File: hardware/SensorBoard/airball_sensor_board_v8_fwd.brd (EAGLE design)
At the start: 5.6 x 9.2 mm, 60 parts, among them IC1 CP2102, J2 USB Female Type C Connector, T1 BC846, T2 BC846, U1 BQ24075, U2 BQ27441-G1, U3 BMP388, U4 ESP-WROOM-32

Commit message: Finished initial design and routing.
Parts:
- removed FID1, FID2, FID3, FID4, FID5, FID6: FIDUCIAL1X2, SparkFun-Aesthetics:FIDUCIAL-1X2
- removed FRAME1, FRAME2: FRAME-LETTER, SparkFun-Aesthetics:CREATIVE_COMMONS
- removed R11: (no value), SparkFun-Resistors:1206
- removed STANDOFF1, STANDOFF10, STANDOFF11, STANDOFF12, STANDOFF2, STANDOFF3, STANDOFF4, STANDOFF5, STANDOFF6, STANDOFF7, STANDOFF8, STANDOFF9: STAND-OFF, SparkFun-Electromechanical:STAND-OFF
- added C10: 10uF, SparkFun-Capacitors:0603
- added C11, C925, C926, C927: 4.7uF, SparkFun-Capacitors:0603
- added C8, C9: 0.1uF, SparkFun-Capacitors:0603
- added R17: 0.01, SparkFun-Resistors:1206
- added U7: SP0503BAHT, SP0503BAHT:SOT143
- R3: value 2.0k -> 1k
- moved FRAME3 148.2 mm to (8.26, -10.2)
- moved R12 132.2 mm to (36.8, 26.4), turned to 180 degrees
- moved R10 130.8 mm to (36.8, 28.3), turned to 180 degrees
- moved R14 121.8 mm to (9.53, 4.13), turned to 270 degrees
- moved R13 120.3 mm to (15.6, 4.13), turned to 270 degrees
- moved T2 116.0 mm to (18.4, 4.13), turned to 180 degrees
- moved U3 112.3 mm to (71.1, 4.45)
- moved T1 106.9 mm to (12.7, 4.13), turned to 180 degrees
- moved U4 100.0 mm to (33.3, 12.1)
- moved C6 77.5 mm to (29.8, 27.3)
- moved R4 68.4 mm to (10.8, 16.8), turned to 270 degrees
- moved R6 68.4 mm to (10.8, 13.3), turned to 90 degrees
- moved C7 62.9 mm to (14.0, 16.2), turned to 180 degrees
- moved J1 60.0 mm to (85.7, 31.4), turned to 90 degrees
- moved R3 58.5 mm to (10.8, 9.53), turned to 90 degrees
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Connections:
- net N$1 renamed MISO
- net N$10 renamed SS_27
- net N$2 renamed SCLK
- net N$6 renamed SS_25
- net N$9 renamed SS_26
- removed net VDD: U3.10
- new net N$14: C6.1, U2.5
- net BATTERY_IN: now also R17.2; no longer R11.2
- net GND: now also C10.2, C11.2, C8.2, C9.2, C925.2, C926.2, C927.2, J1.1, U7.1; no longer J1.2
- net USB_D+: now also U7.3
- net USB_D-: now also U7.2
- net VCC: now also C10.1, C11.1, C8.1, C9.1, C925.1, C926.1, C927.1, J1.2, U3.10; no longer C6.1, J1.1, R3.2, U2.5
- net V_BATT: now also R17.1; no longer R11.1
- net V_USB: now also R3.2, U7.4
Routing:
- net VCC: track 52.9 -> 186.2 mm, vias 2 -> 7
- net SDA: track 0.00 -> 128.1 mm, vias 0 -> 4
- net SCL: track 0.00 -> 125.0 mm, vias 0 -> 6
- net MISO: track 0.00 -> 75.6 mm, vias 0 -> 2
- net SCLK: track 0.00 -> 71.3 mm, vias 0 -> 4
- net V_USB: track 11.0 -> 68.6 mm, vias 0 -> 2
- net SS_26: track 0.00 -> 41.9 mm, vias 0 -> 2
- net N$12: track 0.00 -> 39.5 mm, vias 0 -> 2
- net USB_D-: track 0.00 -> 31.4 mm, vias 0 -> 2
- net SS_27: track 0.00 -> 29.6 mm, vias 0 -> 2
- net USB_D+: track 0.00 -> 29.5 mm, vias 0 -> 2
- net V_BATT: track 8.99 -> 37.5 mm, vias 0 -> 2
- net USB_RXD: track 0.00 -> 26.2 mm, vias 0 -> 2
- net USB_TXD: track 0.00 -> 26.1 mm, vias 0 -> 2
- net BATTERY_IN: track 21.9 -> 47.9 mm, vias 2 -> 3
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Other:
- board text added: "Ihab Awad"

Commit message: Applied design rules and improved the board.
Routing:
- net GND: track 0.00 -> 20.0 mm, vias 0 -> 7
- net BATTERY_IN: track 47.9 -> 51.1 mm
- net USB_D+: track 29.5 -> 31.7 mm
- net USB_D-: track 31.4 -> 33.5 mm
- net V_BATT: track 37.5 -> 38.7 mm
- net V_USB: track 68.6 -> 69.6 mm
- net N$13: track 8.90 -> 8.87 mm, vias 1 -> 2
- added copper zone on layer 1, net GND
- added copper zone on layer 16, net GND

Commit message: More routing and design.
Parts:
- added D2: GREEN, SparkFun-LED:LED-0603
- added D3: Yellow, SparkFun-LED:LED-0603
- added D4: RED, SparkFun-LED:LED-0603
- added R11: 180, SparkFun-Resistors:0603-RES
- added R18: 10K, SparkFun-Resistors:0603-RES
- added R19: 750, SparkFun-Resistors:0603-RES
- R5: value 590 -> 898
- R7: value 1.1k -> 1.54k
- R8: value 100k -> 750
- U$925, U$926, U$927: value HONEYWELL_HSC_SMT -> (none)
- moved U$926 90.6 mm to (157.8, 47.3)
- moved C11 90.6 mm to (156.5, 21.9)
- moved C925 90.6 mm to (146.4, 52.4)
- moved C926 90.6 mm to (164.5, 52.4)
- moved C927 90.6 mm to (147.0, 32.4)
- moved J1 90.6 mm to (174.6, 48.9)
- moved U$927 90.6 mm to (140.3, 27.3)
- moved U3 90.6 mm to (160.0, 21.9)
- moved U$925 90.6 mm to (139.7, 47.3)
- moved FRAME3 57.3 mm to (65.4, -14.6)
- moved R9 34.1 mm to (31.4, 2.54), turned to 270 degrees
- moved R8 30.9 mm to (33.3, 2.54), turned to 270 degrees
- moved D1 28.8 mm to (31.4, 6.03), turned to 270 degrees
- moved C2 28.1 mm to (10.2, 2.54)
- moved R10 27.7 mm to (25.7, 2.86), turned to 90 degrees
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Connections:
- net N$3 renamed SYSOFF_PULLUP
- removed net !CE!: R8.1, U1.4
- removed net EN1: R16.2, U1.6
- new net N$1: D4.A, U4.9
- new net N$19: R11.2, U1.7
- new net N$2: D4.C, R19.1
- new net N$20: D2.C, R11.1
- new net N$21: R16.2, U1.5
- new net N$22: D3.C, R8.1
- new net N$23: R18.2, U2.10
- net GND: now also R18.1, R19.2, U1.4, U1.6; no longer U1.5
- net TS: no longer U2.10
- net VCC: now also D3.A
- net V_SUPPLY_UNREG: now also D2.A
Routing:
- net VCC: track 185.8 -> 65.4 mm, vias 7 -> 0
- net SDA: track 127.9 -> 9.54 mm, vias 4 -> 0
- net SCL: track 125.3 -> 8.37 mm, vias 6 -> 0
- net MISO: track 75.8 -> 0.00 mm, vias 2 -> 0
- net SCLK: track 71.7 -> 0.00 mm, vias 4 -> 0
- net SS_26: track 42.3 -> 0.00 mm, vias 2 -> 0
- net BATTERY_IN: track 51.1 -> 13.9 mm, vias 3 -> 6
- net SS_27: track 29.9 -> 0.00 mm, vias 2 -> 0
- net V_BATT: track 38.7 -> 9.65 mm, vias 2 -> 0
- net SYSOFF_PULLUP: track 3.14 -> 29.9 mm, vias 0 -> 2
- net N$13: track 8.87 -> 33.5 mm
- net SS_25: track 22.1 -> 0.00 mm, vias 2 -> 0
- net N$12: track 39.7 -> 19.6 mm
- net V_SUPPLY_UNREG: track 26.2 -> 6.69 mm
- net !CHG!: track 3.32 -> 21.8 mm, vias 0 -> 2
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- added copper zone on layer 1, net BATTERY_IN
- added copper zone on layer 16, net BATTERY_IN
- added copper zone on layer 1, net V_BATT
- added copper zone on layer 1, net V_SUPPLY_UNREG
- added copper zone on layer 1, net V_USB
- removed copper zone on layer 1, net GND
- removed copper zone on layer 16, net GND

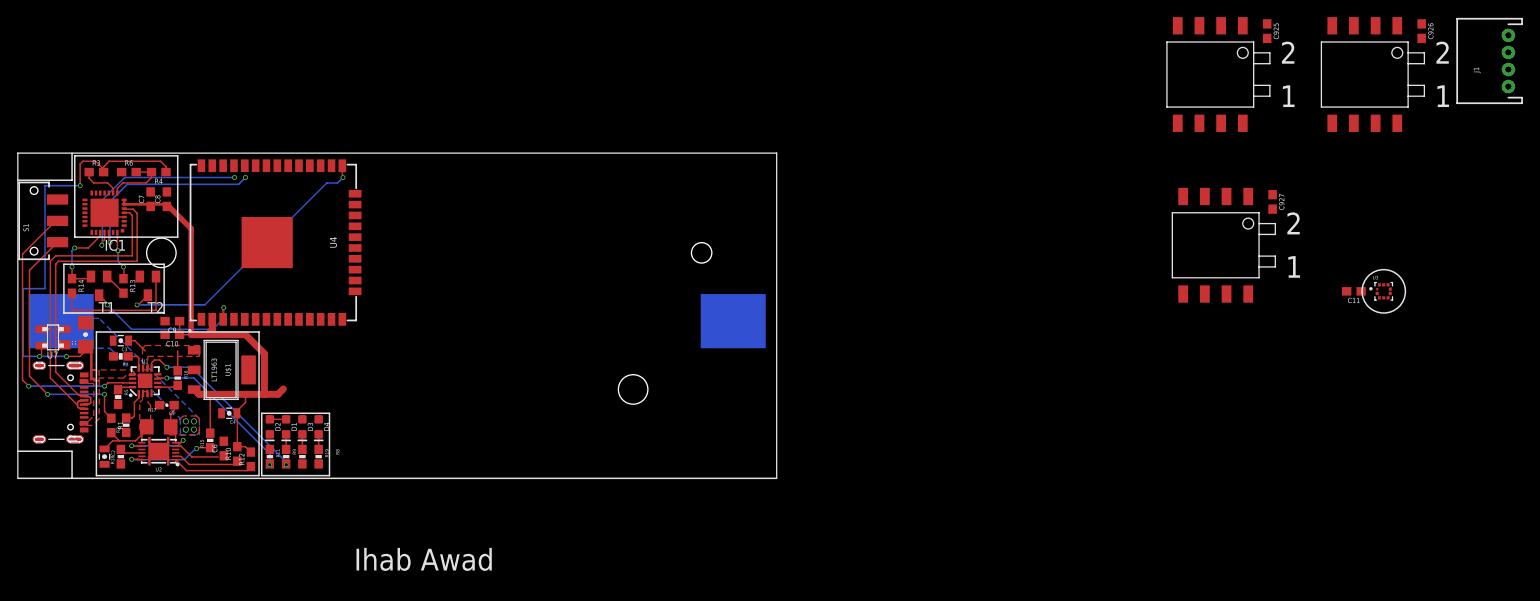
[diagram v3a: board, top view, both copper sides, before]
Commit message: Finished routing board; ground planes still not done.
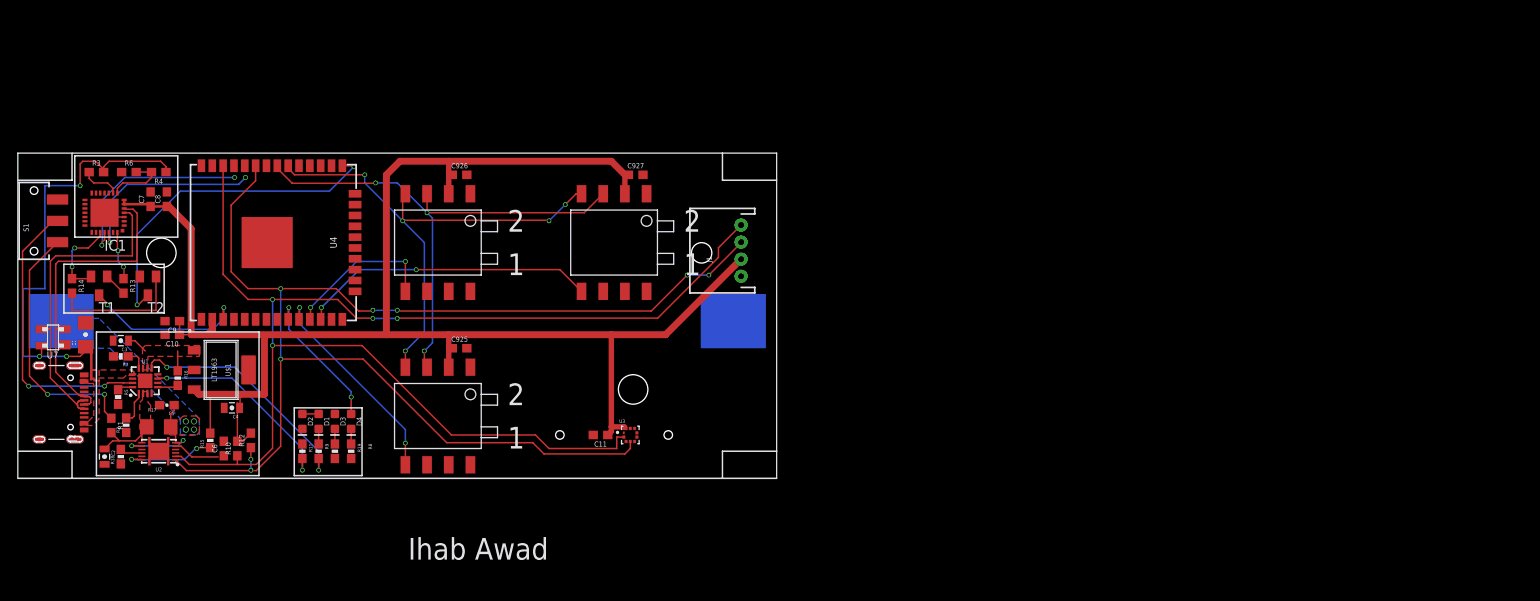
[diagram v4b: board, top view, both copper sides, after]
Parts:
- moved C926 114.0 mm to (51.8, 35.6), turned to 0 degrees
- moved U$926 110.4 mm to (49.2, 27.6)
- moved C925 101.6 mm to (51.8, 15.2), turned to 0 degrees
- moved U$925 98.9 mm to (49.2, 7.30)
- moved J1 92.6 mm to (84.7, 26.7)
- moved U3 89.9 mm to (71.8, 5.08)
- moved C11 89.9 mm to (68.3, 5.08)
- moved C927 74.7 mm to (72.4, 35.6), turned to 0 degrees
- moved U$927 70.5 mm to (69.8, 27.6)
- moved FRAME3 50.5 mm to (15.2, -8.57)
- moved D3 3.86 mm to (37.1, 6.67)
- moved D4 3.86 mm to (39.1, 6.67)
- moved R19 3.86 mm to (39.1, 3.17)
- moved R8 3.86 mm to (37.1, 3.17)
- moved D1 3.86 mm to (35.2, 6.67)
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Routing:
- net SDA: track 9.54 -> 160.5 mm, vias 0 -> 8
- net SCL: track 8.37 -> 159.3 mm, vias 0 -> 4
- net VCC: track 65.4 -> 195.0 mm
- net MISO: track 0.00 -> 62.7 mm, vias 0 -> 3
- net SCLK: track 0.00 -> 61.6 mm, vias 0 -> 5
- net SS_27: track 0.00 -> 34.8 mm, vias 0 -> 2
- net SS_25: track 0.00 -> 25.0 mm, vias 0 -> 2
- net SS_26: track 0.00 -> 18.3 mm, vias 0 -> 2
- net N$1: track 0.00 -> 16.9 mm, vias 0 -> 2
- net N$13: track 33.5 -> 40.1 mm
- net !CHG!: track 21.8 -> 28.4 mm
- net N$19: track 18.1 -> 24.3 mm

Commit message: Updated descriptions and documentation.
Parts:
- added FRAME1, FRAME2: FRAME-LETTER, SparkFun-Aesthetics:CREATIVE_COMMONS
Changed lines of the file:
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@@
 <layer number="14" name="Route14" color="1" fill="6" visible="no" active="no"/>
 <layer number="15" name="Route15" color="4" fill="6" visible="no" active="no"/>
-<layer number="16" name="Bottom" color="1" fill="1" visible="yes" active="yes"/>
+<layer number="16" name="Bottom" color="1" fill="1" visible="no" active="yes"/>
 <layer number="17" name="Pads" color="2" fill="1" visible="yes" active="yes"/>
 <layer number="18" name="Vias" color="2" fill="1" visible="yes" active="yes"/>
@@
 <layer number="20" name="Dimension" color="15" fill="1" visible="yes" active="yes"/>
 <layer number="21" name="tPlace" color="16" fill="1" visible="yes" active="yes"/>
-<layer number="22" name="bPlace" color="14" fill="1" visible="yes" active="yes"/>
+<layer number="22" name="bPlace" color="14" fill="1" visible="no" active="yes"/>
 <layer number="23" name="tOrigins" color="15" fill="1" visible="yes" active="yes"/>
-<layer number="24" name="bOrigins" color="15" fill="1" visible="yes" active="yes"/>
+<layer number="24" name="bOrigins" color="15" fill="1" visible="no" active="yes"/>
 <layer number="25" name="tNames" color="7" fill="1" visible="yes" active="yes"/>
-<layer number="26" name="bNames" color="7" fill="1" visible="yes" active="yes"/>
+<layer number="26" name="bNames" color="7" fill="1" visible="no" active="yes"/>
 <layer number="27" name="tValues" color="7" fill="1" visible="no" active="yes"/>
 <layer number="28" name="bValues" color="7" fill="1" visible="no" active="yes"/>
@@
 <layer number="38" name="bTest" color="7" fill="1" visible="no" active="yes"/>
 <layer number="39" name="tKeepout" color="4" fill="11" visible="yes" active="yes"/>
-<layer number="40" name="bKeepout" color="1" fill="11" visible="yes" active="yes"/>
+<layer number="40" name="bKeepout" color="1" fill="11" visible="no" active="yes"/>
 <layer number="41" name="tRestrict" color="4" fill="10" visible="yes" active="yes"/>
-<layer number="42" name="bRestrict" color="1" fill="10" visible="yes" active="yes"/>
+<layer number="42" name="bRestrict" color="1" fill="10" visible="no" active="yes"/>
 <layer number="43" name="vRestrict" color="2" fill="10" visible="no" active="yes"/>
 <layer number="44" name="Drills" color="7" fill="1" visible="no" active="yes"/>
-<layer number="45" name="Holes" color="7" fill="1" visible="yes" active="yes"/>
+<layer number="45" name="Holes" color="7" fill="1" visible="no" active="yes"/>
 <layer number="46" name="Milling" color="3" fill="1" visible="no" active="yes"/>
 <layer number="47" name="Measures" color="7" fill="1" visible="no" active="yes"/>
@@
 <layer number="50" name="dxf" color="7" fill="1" visible="no" active="no"/>
 <layer number="51" name="tDocu" color="6" fill="1" visible="yes" active="yes"/>
-<layer number="52" name="bDocu" color="7" fill="1" visible="yes" active="yes"/>
+<layer number="52" name="bDocu" color="7" fill="1" visible="no" active="yes"/>
 <layer number="53" name="tGND_GNDA" color="7" fill="9" visible="no" active="no"/>
 <layer number="54" name="bGND_GNDA" color="1" fill="9" visible="no" active="no"/>
@@
 <attribute name="VALUE" x="37.9095" y="4.191" size="0.4064" layer="27" font="vector" rot="R270"/>
 </element>
+<element name="FRAME1" library="SparkFun-Aesthetics" package="CREATIVE_COMMONS" value="FRAME-LETTER" x="6.985" y="-21.59" smashed="yes"/>
+<element name="FRAME2" library="SparkFun-Aesthetics" package="CREATIVE_COMMONS" value="FRAME-LETTER" x="6.985" y="-30.1625" smashed="yes"/>
 </elements>
 <signals>
